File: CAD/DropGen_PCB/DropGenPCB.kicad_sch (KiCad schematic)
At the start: 24 parts, among them J1 JST_3_pin, J2 JST_4_pin, J3 Barrel_Jack_Switch, J4 Camera Terminal Block, J5 Piezo, U1 SEEED XIAO ESP32S3, U2 TMC2209_SILENTSTEPSTICK, U3 L293D, U4 TPS5430DDAR

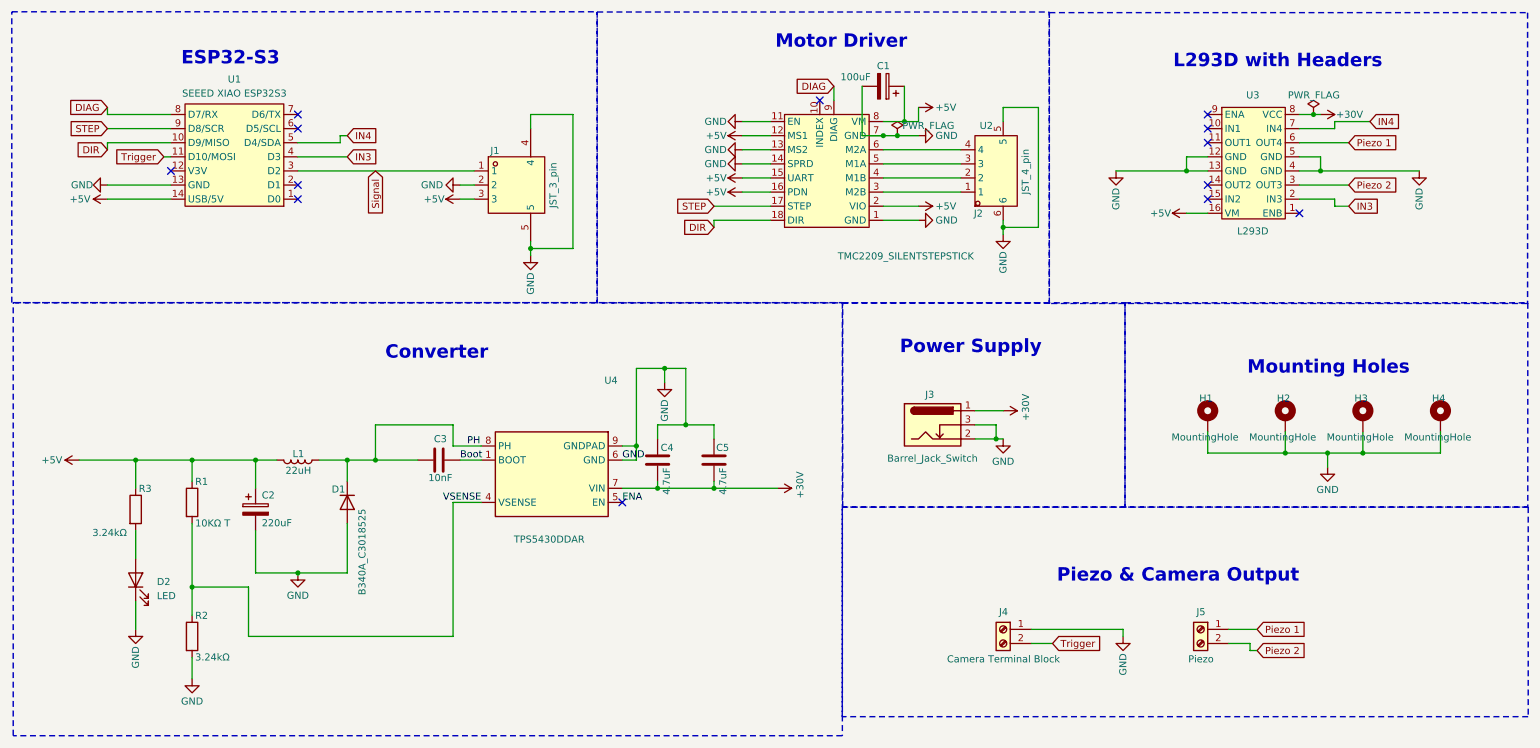
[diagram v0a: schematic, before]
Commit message: updated components to current stock on JLCPCB
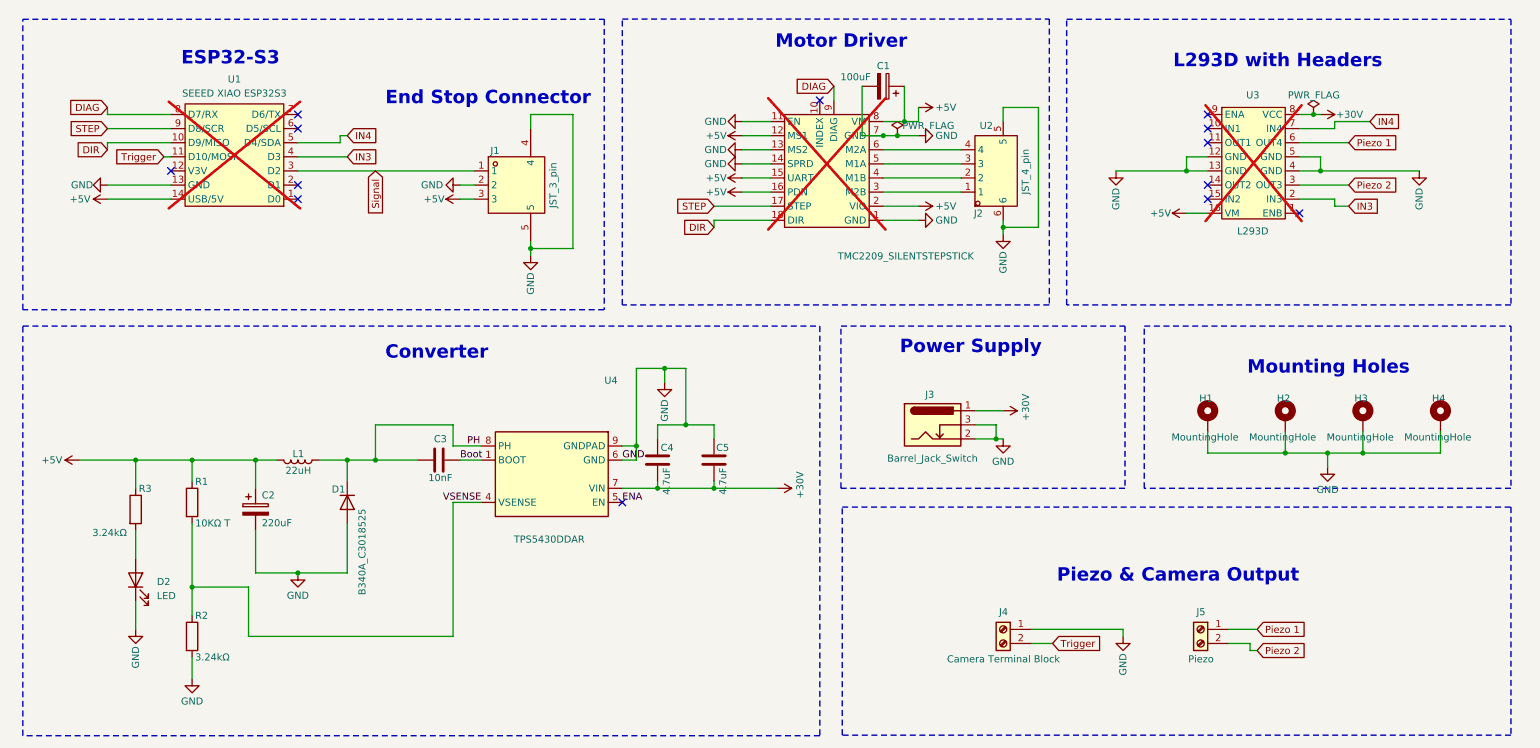
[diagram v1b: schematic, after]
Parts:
- J1: LCSC C161860 -> C5306495
- L1: value 22uH -> 22uH
- U1, U2, U3: now not fitted; now left out of the parts list
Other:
- note added: "End Stop Connector"
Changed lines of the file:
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@@
 (kicad_sch
-	(version 20231120)
+	(version 20250114)
 	(generator "eeschema")
-	(generator_version "8.0")
+	(generator_version "9.0")
 	(paper "A4")
+	(rectangle
+		(start 13.97 13.335)
+		(end 118.6626 65.6304)
+		(stroke
+			(width 0.254)
+			(type dash)
+		)
+		(fill
+			(type none)
+		)
+	)
+	(rectangle
+		(start 161.5227 101.1712)
+		(end 281.94 142.24)
+		(stroke
+			(width 0.254)
+			(type dash)
+		)
+		(fill
+			(type none)
+		)
+	)
+	(rectangle
+		(start 121.92 13.2924)
+		(end 198.8103 64.77)
+		(stroke
+			(width 0.254)
+			(type dash)
+		)
+		(fill
+			(type none)
+		)
+	)
+	(rectangle
+		(start 161.29 68.58)
+		(end 212.4369 97.79)
+		(stroke
+			(width 0.254)
+			(type dash)
+		)
+		(fill
+			(type none)
+		)
+	)
+	(rectangle
+		(start 215.9 68.58)
+		(end 281.94 97.79)
+		(stroke
+			(width 0.254)
+			(type dash)
+		)
+		(fill
+			(type none)
+		)
+	)
+	(rectangle
+		(start 13.97 68.58)
+		(end 157.48 142.3383)
+		(stroke
+			(width 0.254)
+			(type dash)
+		)
+		(fill
+			(type none)
+		)
+	)
+	(rectangle
+		(start 201.93 13.335)
+		(end 281.94 64.77)
+		(stroke
+			(width 0.254)
+			(type dash)
+		)
+		(fill
+			(type none)
+		)
+	)
+	(text "Mounting Holes"
+		(exclude_from_sim no)
+		(at 234.442 74.676 0)
+		(effects
+			(font
+				(face "KiCad Font")
+				(size 2.413 2.413)
+				(thickness 0.4826)
+				(bold yes)
+			)
+			(justify left top)
+		)
+	)
+	(text "ESP32-S3"
+		(exclude_from_sim no)
+		(at 42.4915 18.9962 0)
+		(effects
+			(font
+				(face "KiCad Font")
+				(size 2.413 2.413)
+				(thickness 0.4826)
+				(bold yes)
+			)
+			(justify left top)
+		)
+	)
+	(text "Converter"
+		(exclude_from_sim no)
+		(at 79.2272 71.9856 0)
+		(effects
+			(font
+				(face "KiCad Font")
+				(size 2.413 2.413)
+				(thickness 0.4826)
+				(bold yes)
+			)
+			(justify left top)
+		)
+	)
+	(text "Motor Driver"
+		(exclude_from_sim no)
+		(at 149.4701 15.9968 0)
+		(effects
+			(font
+				(face "KiCad Font")
+				(size 2.413 2.413)
+				(thickness 0.4826)
+				(bold yes)
+			)
+			(justify left top)
+		)
+	)
+	(text "End Stop Connector"
+		(exclude_from_sim no)
+		(at 79.248 26.162 0)
+		(effects
+			(font
+				(face "KiCad Font")
+				(size 2.413 2.413)
+				(thickness 0.4826)
+				(bold yes)
+			)
+			(justify left top)
+		)
+	)
+	(text "Piezo & Camera Output"
+		(exclude_from_sim no)
+		(at 200.1758 112.1263 0)
+		(effects
+			(font
+				(face "KiCad Font")
+				(size 2.413 2.413)
+				(thickness 0.4826)
+				(bold yes)
+			)
+			(justify left top)
+		)
+	)
+	(text "L293D with Headers"
+		(exclude_from_sim no)
+		(at 221.1178 19.4961 0)
+		(effects
+			(font
+				(face "KiCad Font")
+				(size 2.413 2.413)
+				(thickness 0.4826)
+				(bold yes)
+			)
+			(justify left top)
+		)
+	)
+	(text "Power Supply"
+		(exclude_from_sim no)
+		(at 171.8846 70.9858 0)
+		(effects
+			(font
+				(face "KiCad Font")
+				(size 2.413 2.413)
+				(thickness 0.4826)
+				(bold yes)
+			)
+			(justify left top)
+		)
+	)
 	(junction
 		(at 133.35 86.36)
@@
 		)
 	)
-	(rectangle
-		(start 11.9876 11.9876)
-		(end 117.3926 64.3604)
-		(stroke
-			(width 0.254)
-			(type dash)
-		)
-		(fill
-			(type none)
-		)
-	)
-	(rectangle
-		(start 161.5227 101.1712)
-		(end 285.038 138.9102)
-		(stroke
-			(width 0.254)
-			(type dash)
-		)
-		(fill
-			(type none)
-		)
-	)
-	(rectangle
-		(start 117.3926 12.0224)
-		(end 198.8103 64.3952)
-		(stroke
-			(width 0.254)
-			(type dash)
-		)
-		(fill
-			(type none)
-		)
-	)
-	(rectangle
-		(start 161.6004 64.3981)
-		(end 212.4369 101.1686)
-		(stroke
-			(width 0.254)
-			(type dash)
-		)
-		(fill
-			(type none)
-		)
-	)
-	(rectangle
-		(start 212.4369 64.4007)
-		(end 284.9665 101.1712)
-		(stroke
-			(width 0.254)
-			(type dash)
-		)
-		(fill
-			(type none)
-		)
-	)
-	(rectangle
-		(start 12.2382 64.3604)
-		(end 161.5432 142.3383)
-		(stroke
-			(width 0.254)
-			(type dash)
-		)
-		(fill
-			(type none)
-		)
-	)
-	(rectangle
-		(start 198.8103 12.1394)
-		(end 284.9275 64.5122)
-		(stroke
-			(width 0.254)
-			(type dash)
-		)
-		(fill
-			(type none)
-		)
-	)
-	(text "Mounting Holes"
-		(exclude_from_sim no)
-		(at 234.442 74.676 0)
-		(effects
-			(font
-				(face "KiCad Font")
-				(size 2.413 2.413)
-				(thickness 0.4826)
-				(bold yes)
-			)
-			(justify left top)
-		)
-	)
-	(text "ESP32-S3"
-		(exclude_from_sim no)
-		(at 42.4915 18.9962 0)
-		(effects
-			(font
-				(face "KiCad Font")
-				(size 2.413 2.413)
-				(thickness 0.4826)
-				(bold yes)
-			)
-			(justify left top)
-		)
-	)
-	(text "Converter"
-		(exclude_from_sim no)
-		(at 79.2272 71.9856 0)
-		(effects
-			(font
-				(face "KiCad Font")
-				(size 2.413 2.413)
-				(thickness 0.4826)
-				(bold yes)
-			)
-			(justify left top)
-		)
-	)
-	(text "Motor Driver"
-		(exclude_from_sim no)
-		(at 149.4701 15.9968 0)
-		(effects
-			(font
-				(face "KiCad Font")
-				(size 2.413 2.413)
-				(thickness 0.4826)
-				(bold yes)
-			)
-			(justify left top)
-		)
-	)
-	(text "Piezo & Camera Output"
-		(exclude_from_sim no)
-		(at 200.1758 112.1263 0)
-		(effects
-			(font
-				(face "KiCad Font")
-				(size 2.413 2.413)
-				(thickness 0.4826)
-				(bold yes)
-			)
-			(justify left top)
-		)
-	)
-	(text "L293D with Headers"
-		(exclude_from_sim no)
-		(at 221.1178 19.4961 0)
-		(effects
-			(font
-				(face "KiCad Font")
-				(size 2.413 2.413)
-				(thickness 0.4826)
-				(bold yes)
-			)
-			(justify left top)
-		)
-	)
-	(text "Power Supply"
-		(exclude_from_sim no)
-		(at 171.8846 70.9858 0)
-		(effects
-			(font
-				(face "KiCad Font")
-				(size 2.413 2.413)
-				(thickness 0.4826)
-				(bold yes)
-			)
-			(justify left top)
-		)
-	)
 	(label "Boot"
 		(at 92.71 92.71 0)
-		(fields_autoplaced yes)
 		(effects
 			(font
@@
 	(label "GND"
 		(at 121.92 92.71 0)
-		(fields_autoplaced yes)
 		(effects
 			(font
@@
 	(label "VSENSE"
 		(at 96.52 100.33 180)
-		(fields_autoplaced yes)
 		(effects
 			(font
@@
 	(label "ENA"
 		(at 121.92 100.33 0)
-		(fields_autoplaced yes)
 		(effects
 			(font
@@
 	(label "PH"
 		(at 93.98 90.17 0)
-		(fields_autoplaced yes)
 		(effects
 			(font
@@
 			)
 		)
-		(property "Description" " 2.5 5mm 12~28 1x2P 15A 2P 300V Gray 2 1 Plugin,P=5mm Spring Clamp System Terminal Block ROHS"
+		(property "Description" "2.5 5mm 12~28 1x2P 15A 2P 300V Gray 2 1 Plugin,P=5mm Spring Clamp System Terminal Block ROHS"
 			(at 190.5 123.19 0)
 			(effects
@@
 		(unit 1)
 		(exclude_from_sim no)
-		(in_bom yes)
+		(in_bom no)
 		(on_board yes)
-		(dnp no)
+		(dnp yes)
 		(property "Reference" "U3"
 			(at 235.4529 26.9946 0)
@@
 		(unit 1)
 		(exclude_from_sim no)
-		(in_bom yes)
+		(in_bom no)
 		(on_board yes)
-		(dnp no)
+		(dnp yes)
 		(fields_autoplaced yes)
 		(property "Reference" "U1"
@@
 			)
 		)
-		(property "Value" "22uH "
+		(property "Value" "22uH"
 			(at 63.5816 94.5893 90)
 			(effects
@@
 		(unit 1)
 		(exclude_from_sim no)
-		(in_bom yes)
+		(in_bom no)
 		(on_board yes)
-		(dnp no)
+		(dnp yes)
 		(property "Reference" "U2"
 			(at 187.4625 32.4935 0)
@@
 			)
 		)
-		(property "Description" " 60V 700mV@5A 5A SMC(DO-214AB) Schottky Diodes ROHS "
+		(property "Description" "60V 700mV@5A 5A SMC(DO-214AB) Schottky Diodes ROHS"
 			(at 72.39 100.33 0)
 			(effects
@@
 			)
 		)
-		(property "Datasheet" "https://www.lcsc.com/datasheet/lcsc_datasheet_2304140030_JST-S3B-XH-SM4-TB-LF-SN_C161860.pdf"
+		(property "Datasheet" "https://www.lcsc.com/datasheet/C5306495.pdf?spm=wm.sxq.inf.ggs&lcsc_vid=QVBbUFwER1lfVAAAFVZbBQZRR1kPXlJeRQMPXlEARQAxVlNeQlZZUlZSQlRYUjsOAxUeFF5JWBYZEEoKFBINSQcJGk4NBhADEA4cHktRTlNADxALGw%3D%3D"
 			(at 99.06 36.83 0)
 			(effects
@@
 			)
 		)
-		(property "LCSC" "C161860"
+		(property "LCSC" "C5306495"
 			(at 97.79 38.1 0)
 			(effects
@@
 			)
 		)
-		(property "Description" " Bend insert DC Power Receptacle -40℃~+55℃ 2.1mm 6.3mm 500mA 30V Plugin DC Power Connectors ROHS"
+		(property "Description" "Bend insert DC Power Receptacle -40℃~+55℃ 2.1mm 6.3mm 500mA 30V Plugin DC Power Connectors ROHS"
 			(at 177.8 86.36 0)
 			(effects
@@
 			)
 		)
-		(property "Description" " 2.5 5mm 12~28 1x2P 15A 2P 300V Gray 2 1 Plugin,P=5mm Spring Clamp System Terminal Block ROHS"
+		(property "Description" "2.5 5mm 12~28 1x2P 15A 2P 300V Gray 2 1 Plugin,P=5mm Spring Clamp System Terminal Block ROHS"
 			(at 226.06 123.19 0)
 			(effects
@@
 		)
 	)
+	(embedded_fonts no)
 )

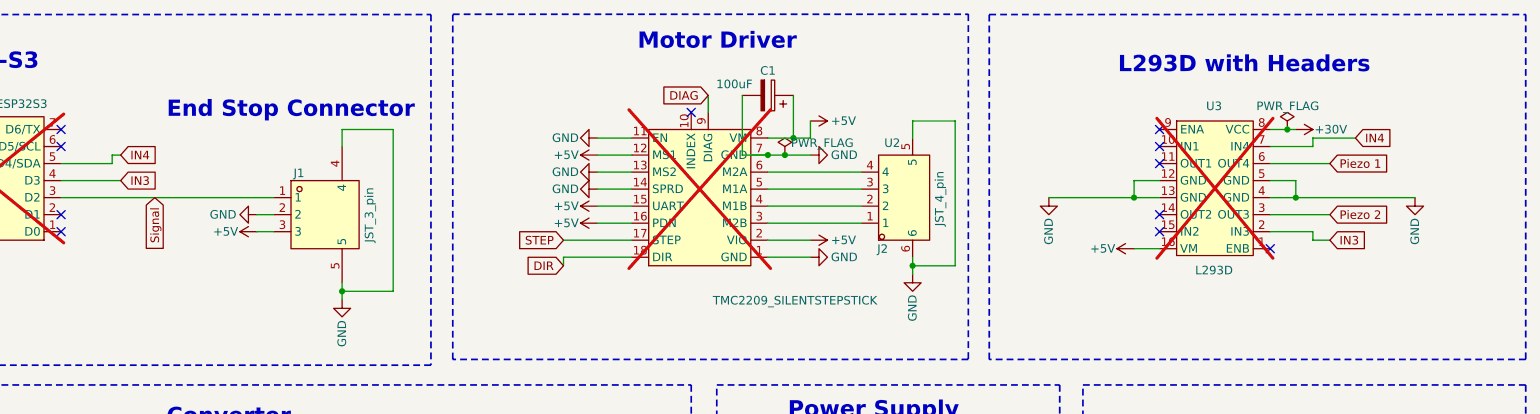
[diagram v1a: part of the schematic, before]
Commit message: now saves values locally between restarts.
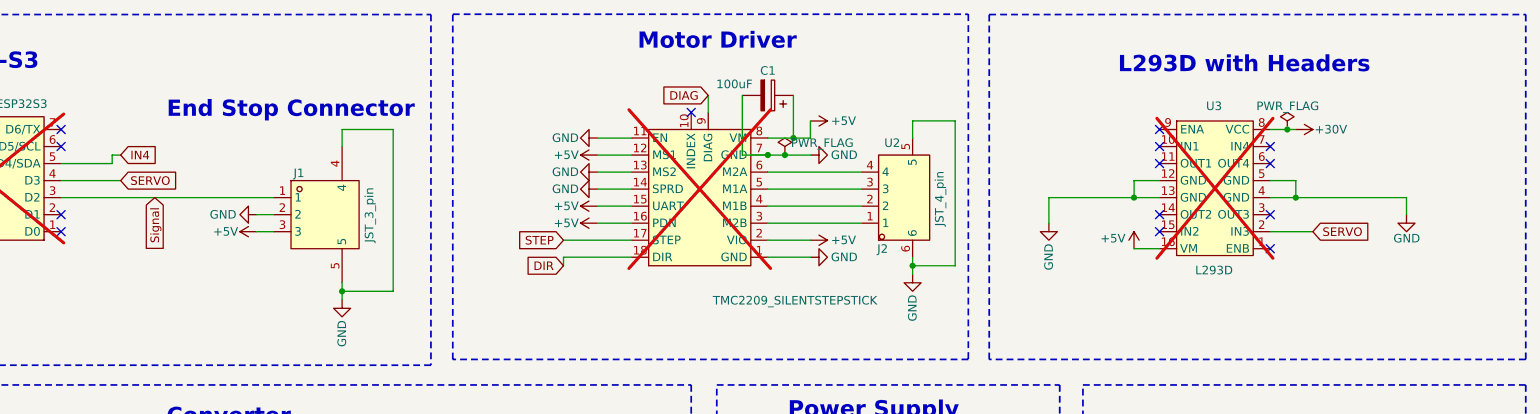
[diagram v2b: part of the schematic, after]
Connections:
- net IN4: no longer U3.7 (IN4)
- net Piezo 1: no longer U3.6 (OUT4)
- net Piezo 2: no longer U3.3 (OUT3)
- net IN3 renamed SERVO
- no-connect marks 13 -> 16
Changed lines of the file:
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@@
 	)
 	(no_connect
+		(at 243.84 35.56)
+	)
+	(no_connect
 		(at 157.48 27.94)
 	)
 	(no_connect
+		(at 243.84 33.02)
+	)
+	(no_connect
 		(at 63.5 45.72)
 	)
@@
 	)
 	(no_connect
+		(at 243.84 43.18)
+	)
+	(no_connect
 		(at 63.5 30.48)
 	)
@@
 	(wire
 		(pts
-			(xy 250.19 45.72) (xy 250.19 46.99)
-		)
-		(stroke
-			(width 0)
-			(type default)
-		)
-	)
-	(wire
-		(pts
 			(xy 24.13 92.71) (xy 34.29 92.71)
 		)
@@
 	(wire
 		(pts
+			(xy 210.82 40.64) (xy 210.82 44.45)
+		)
+		(stroke
+			(width 0)
+			(type default)
+		)
+	)
+	(wire
+		(pts
 			(xy 190.5 29.21) (xy 190.5 31.75)
 		)
@@
 	(wire
 		(pts
-			(xy 250.19 31.75) (xy 256.54 31.75)
-		)
-		(stroke
-			(width 0)
-			(type default)
-		)
-	)
-	(wire
-		(pts
 			(xy 227.33 87.63) (xy 227.33 91.44)
 		)
@@
 	(wire
 		(pts
-			(xy 243.84 33.02) (xy 250.19 33.02)
-		)
-		(stroke
-			(width 0)
-			(type default)
-		)
-	)
-	(wire
-		(pts
 			(xy 182.88 36.83) (xy 168.91 36.83)
 		)
@@
 	(wire
 		(pts
-			(xy 243.84 43.18) (xy 252.73 43.18)
-		)
-		(stroke
-			(width 0)
-			(type default)
-		)
-	)
-	(wire
-		(pts
 			(xy 72.39 96.52) (xy 72.39 92.71)
 		)
@@
 	(wire
 		(pts
+			(xy 264.16 40.64) (xy 264.16 43.18)
+		)
+		(stroke
+			(width 0)
+			(type default)
+		)
+	)
+	(wire
+		(pts
 			(xy 210.82 40.64) (xy 223.52 40.64)
 		)
@@
 	(wire
 		(pts
-			(xy 250.19 46.99) (xy 252.73 46.99)
-		)
-		(stroke
-			(width 0)
-			(type default)
-		)
-	)
-	(wire
-		(pts
 			(xy 128.27 96.52) (xy 128.27 97.79)
 		)
@@
 	(wire
 		(pts
-			(xy 243.84 35.56) (xy 252.73 35.56)
-		)
-		(stroke
-			(width 0)
-			(type default)
-		)
-	)
-	(wire
-		(pts
 			(xy 190.5 88.9) (xy 189.23 88.9)
 		)
@@
 	(wire
 		(pts
-			(xy 250.19 33.02) (xy 250.19 31.75)
-		)
-		(stroke
-			(width 0)
-			(type default)
-		)
-	)
-	(wire
-		(pts
 			(xy 243.84 38.1) (xy 247.65 38.1)
 		)
@@
 	(wire
 		(pts
-			(xy 247.65 40.64) (xy 265.43 40.64)
+			(xy 247.65 40.64) (xy 264.16 40.64)
 		)
 		(stroke
@@
 		)
 	)
-	(global_label "IN3"
+	(global_label "SERVO"
 		(shape input)
 		(at 72.39 38.1 0)
@@
 		)
 		(property "Intersheetrefs" "${INTERSHEET_REFS}"
-			(at 78.52 38.1 0)
+			(at 81.4228 38.1 0)
 			(effects
 				(font
@@
 		)
 	)
-	(global_label "IN4"
-		(shape input)
-		(at 256.54 31.75 0)
-		(fields_autoplaced yes)
-		(effects
-			(font
-				(size 1.27 1.27)
-			)
-			(justify left)
-		)
-		(property "Intersheetrefs" "${INTERSHEET_REFS}"
-			(at 262.67 31.75 0)
-			(effects
-				(font
-					(size 1.27 1.27)
-				)
-				(justify left)
-				(hide yes)
-			)
-		)
-	)
 	(global_label "DIAG"
 		(shape input)
@@
 		)
 	)
-	(global_label "Piezo 1"
-		(shape input)
-		(at 252.73 35.56 0)
-		(fields_autoplaced yes)
-		(effects
-			(font
-				(size 1.27 1.27)
-			)
-			(justify left)
-		)
-		(property "Intersheetrefs" "${INTERSHEET_REFS}"
-			(at 263.0328 35.56 0)
-			(effects
-				(font
-					(size 1.27 1.27)
-				)
-				(justify left)
-				(hide yes)
-			)
-		)
-	)
 	(global_label "DIR"
 		(shape input)
@@
 		)
 	)
-	(global_label "IN3"
+	(global_label "SERVO"
 		(shape input)
-		(at 252.73 46.99 0)
+		(at 250.19 45.72 0)
 		(fields_autoplaced yes)
 		(effects
@@
 		)
 		(property "Intersheetrefs" "${INTERSHEET_REFS}"
-			(at 258.86 46.99 0)
+			(at 259.2228 45.72 0)
 			(effects
 				(font
@@
 		)
 	)
-	(global_label "Piezo 2"
-		(shape input)
-		(at 252.73 43.18 0)
-		(fields_autoplaced yes)
-		(effects
-			(font
-				(size 1.27 1.27)
-			)
-			(justify left)
-		)
-		(property "Intersheetrefs" "${INTERSHEET_REFS}"
-			(at 263.0328 43.18 0)
-			(effects
-				(font
-					(size 1.27 1.27)
-				)
-				(justify left)
-				(hide yes)
-			)
-		)
-	)
 	(global_label "DIR"
 		(shape input)
@@
 	(symbol
 		(lib_id "power:+5V")
-		(at 223.52 48.26 90)
-		(mirror x)
+		(at 223.52 48.26 0)
+		(mirror y)
 		(unit 1)
 		(exclude_from_sim no)
@@
 		(dnp no)
 		(property "Reference" "#PWR025"
-			(at 227.33 48.26 0)
+			(at 223.52 52.07 0)
 			(effects
 				(font
@@
 		)
 		(property "Value" "+5V"
-			(at 220.726 48.26 90)
+			(at 222.25 46.736 0)
 			(effects
 				(font
@@
 	(symbol
 		(lib_id "power:GND")
-		(at 265.43 40.64 0)
+		(at 264.16 43.18 0)
 		(unit 1)
 		(exclude_from_sim no)
@@
 		(dnp no)
 		(property "Reference" "#PWR011"
-			(at 265.43 46.99 0)
+			(at 264.16 49.53 0)
 			(effects
 				(font
@@
 		)
 		(property "Value" "GND"
-			(at 265.43 43.688 90)
+			(at 266.192 46.736 0)
 			(effects
 				(font
@@
 		)
 		(property "Footprint" ""
-			(at 265.43 40.64 0)
+			(at 264.16 43.18 0)
 			(effects
 				(font
@@
 		)
 		(property "Datasheet" ""
-			(at 265.43 40.64 0)
+			(at 264.16 43.18 0)
 			(effects
 				(font
@@
 		)
 		(property "Description" "Power symbol creates a global label with name \"GND\" , ground"
-			(at 265.43 40.64 0)
+			(at 264.16 43.18 0)
 			(effects
 				(font
@@
 	(symbol
 		(lib_id "power:GND")
-		(at 210.82 40.64 0)
+		(at 210.82 44.45 0)
 		(mirror y)
 		(unit 1)
@@
 		(dnp no)
 		(property "Reference" "#PWR028"
-			(at 210.82 46.99 0)
+			(at 210.82 50.8 0)
 			(effects
 				(font
@@
 		)
 		(property "Value" "GND"
-			(at 210.82 43.688 90)
+			(at 210.82 47.498 90)
 			(effects
 				(font
@@
 		)
 		(property "Footprint" ""
-			(at 210.82 40.64 0)
+			(at 210.82 44.45 0)
 			(effects
 				(font
@@
 		)
 		(property "Datasheet" ""
-			(at 210.82 40.64 0)
+			(at 210.82 44.45 0)
 			(effects
 				(font
@@
 		)
 		(property "Description" "Power symbol creates a global label with name \"GND\" , ground"
-			(at 210.82 40.64 0)
+			(at 210.82 44.45 0)
 			(effects
 				(font
